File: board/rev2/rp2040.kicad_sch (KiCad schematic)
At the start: 2 parts, among them U13 TLV74311, U5 RP2354B

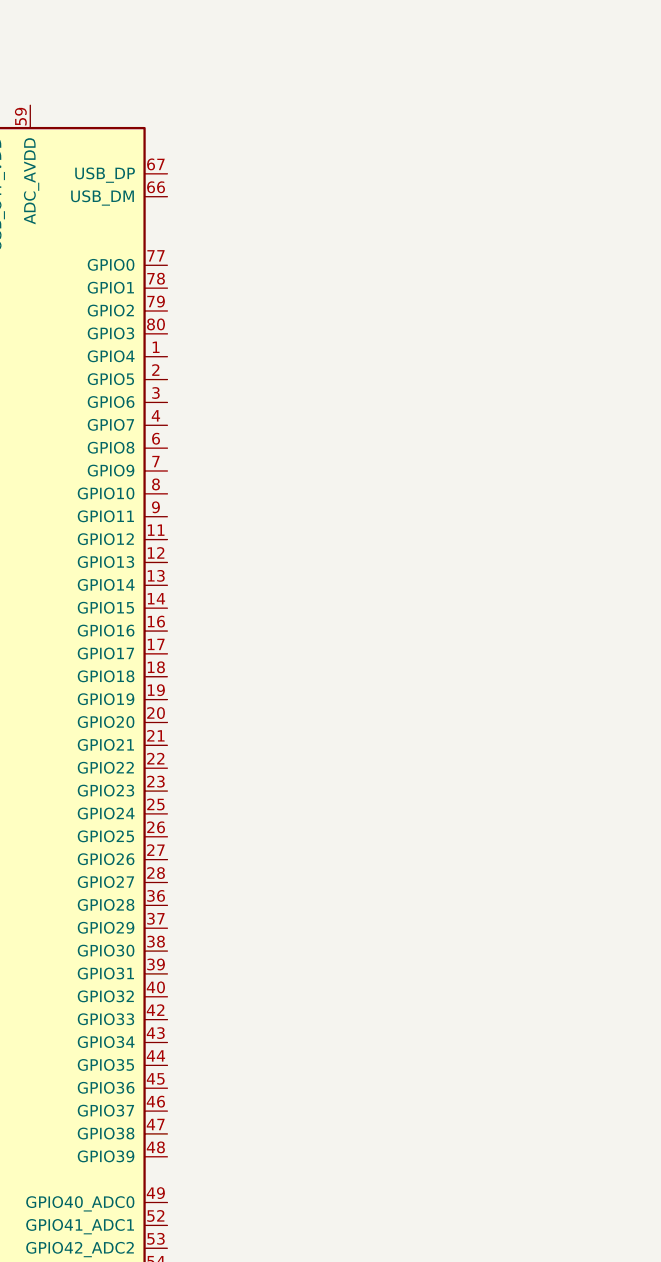
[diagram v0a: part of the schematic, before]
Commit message: Split out board into A/B
allow 2x displays (for chaining)
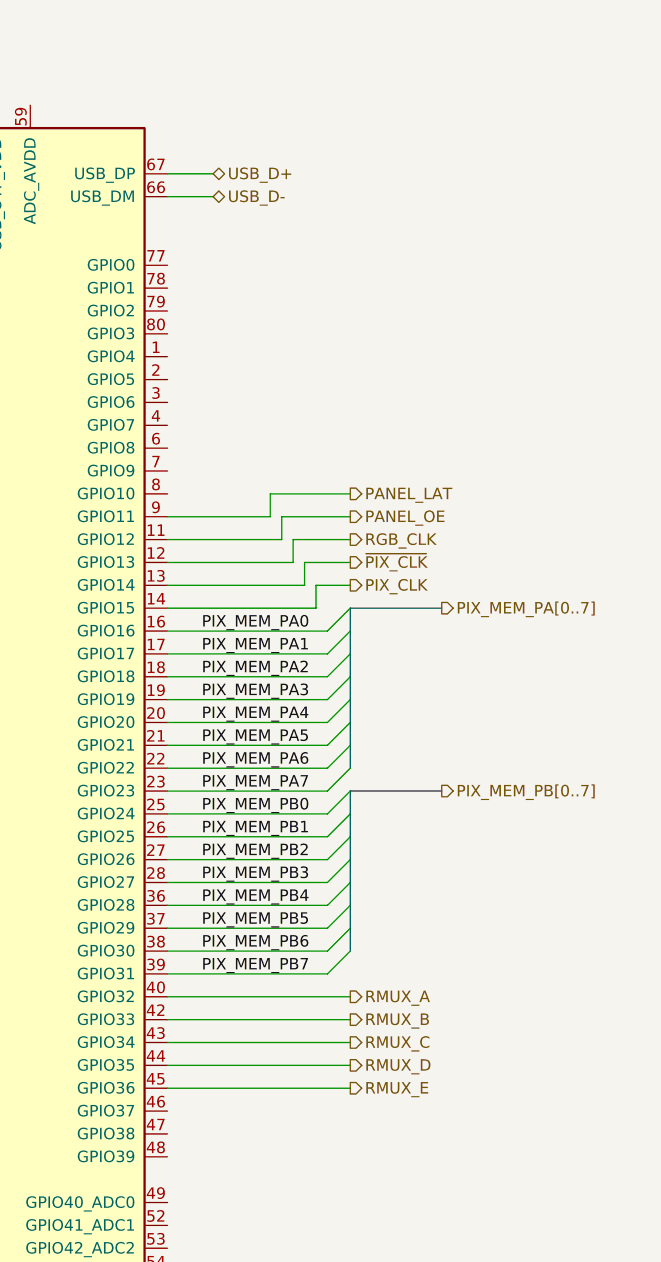
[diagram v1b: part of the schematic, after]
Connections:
- net PANEL_OE: now reaches U5.11 (GPIO12)
- net RGB_CLK: now reaches U5.12 (GPIO13)
- net ~{PIX_CLK}: now reaches U5.13 (GPIO14)
- net PIX_CLK: now reaches U5.14 (GPIO15)
- net PIX_MEM_PA0: now reaches U5.16 (GPIO16)
- net PIX_MEM_PA1: now reaches U5.17 (GPIO17)
- net PIX_MEM_PA2: now reaches U5.18 (GPIO18)
- net PIX_MEM_PA3: now reaches U5.19 (GPIO19)
- net PIX_MEM_PA4: now reaches U5.20 (GPIO20)
- net PIX_MEM_PA5: now reaches U5.21 (GPIO21)
- net PIX_MEM_PA6: now reaches U5.22 (GPIO22)
- net PIX_MEM_PA7: now reaches U5.23 (GPIO23)
- net PIX_MEM_PB0: now reaches U5.25 (GPIO24)
- net PIX_MEM_PB1: now reaches U5.26 (GPIO25)
- net PIX_MEM_PB2: now reaches U5.27 (GPIO26)
- net PIX_MEM_PB3: now reaches U5.28 (GPIO27)
- net PIX_MEM_PB4: now reaches U5.36 (GPIO28)
- net PIX_MEM_PB5: now reaches U5.37 (GPIO29)
- net PIX_MEM_PB6: now reaches U5.38 (GPIO30)
- net PIX_MEM_PB7: now reaches U5.39 (GPIO31)
- net RMUX_A: now reaches U5.40 (GPIO32)
- net RMUX_B: now reaches U5.42 (GPIO33)
- net RMUX_C: now reaches U5.43 (GPIO34)
- net RMUX_D: now reaches U5.44 (GPIO35)
- net RMUX_E: now reaches U5.45 (GPIO36)
- net USB_D-: now reaches U5.66 (USB_DM)
- net USB_D+: now reaches U5.67 (USB_DP)
- net PANEL_LAT: now reaches U5.9 (GPIO11)

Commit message: More board work
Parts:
- added R30, R31: 10k, symbol Device:R_Small_US
- added R32: 1k, symbol Device:R_Small_US
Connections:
- net DAT0: now reaches U5.1 (GPIO4)
- net DAT3: now reaches U5.2 (GPIO5)
- net CLK: now reaches U5.3 (GPIO6)
- net CLK: now also U5.53 (GPIO42_ADC2)
- net CMD: now reaches U5.4 (GPIO7)
- net at U5.46 (GPIO37): now also R32.1
- net MEMA_WE: now reaches U5.47 (GPIO38)
- net MEMA_WE: now also R30.2
- net MEMB_WE: now reaches U5.48 (GPIO39)
- net MEMB_WE: now also R31.2
- net CS: now reaches U5.52 (GPIO41_ADC1)
- net Q0: now reaches U5.54 (GPIO43_ADC3)
- net Q1: now reaches U5.55 (GPIO44_ADC4)
- net Q2: now reaches U5.56 (GPIO45_ADC5)
- net Q3: now reaches U5.57 (GPIO46_ADC6)
- net PIX_CNT_DIN0: now reaches U5.77 (GPIO0)
- net PIX_CNT_DIN1: now reaches U5.78 (GPIO1)
- net PIX_CNT_DIN2: now reaches U5.79 (GPIO2)
- net PIX_CNT_DIN3: now reaches U5.80 (GPIO3)
- new net MEM_IO: R32.2
- new net VDD: R30.1, R31.1

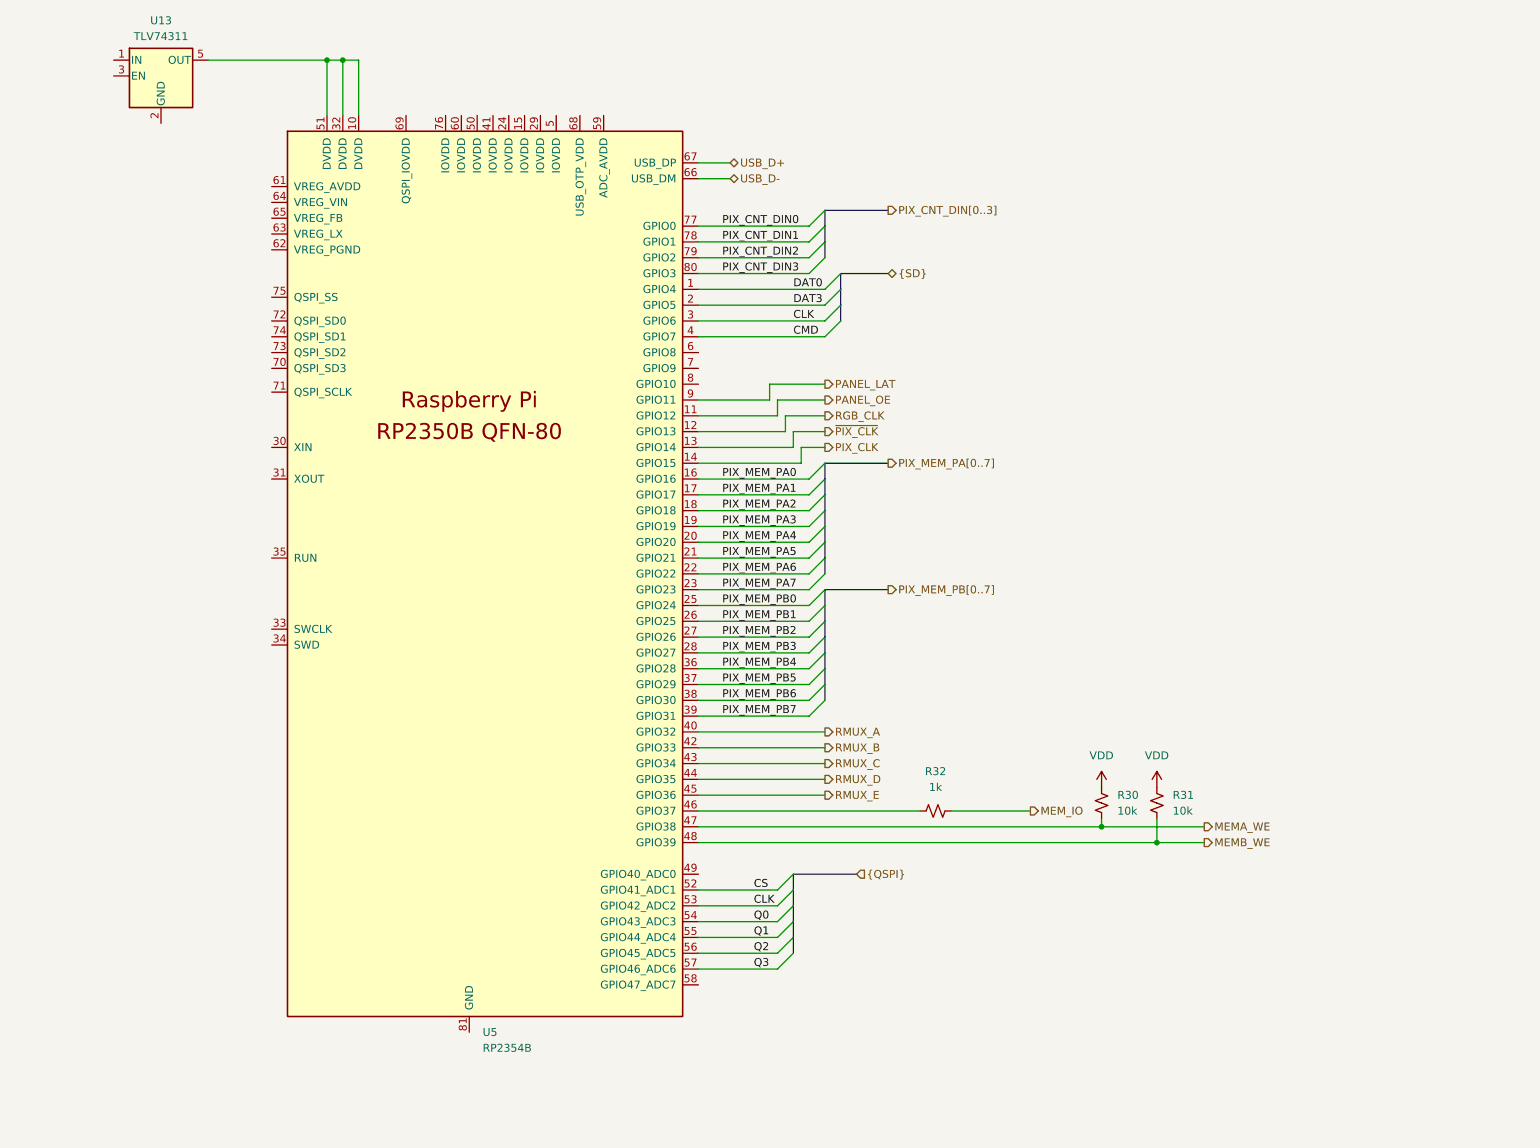
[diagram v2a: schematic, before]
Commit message: Board GPIO allocation
- and usbmux

still need to do termination on the big buses + a bunch of bypass caps
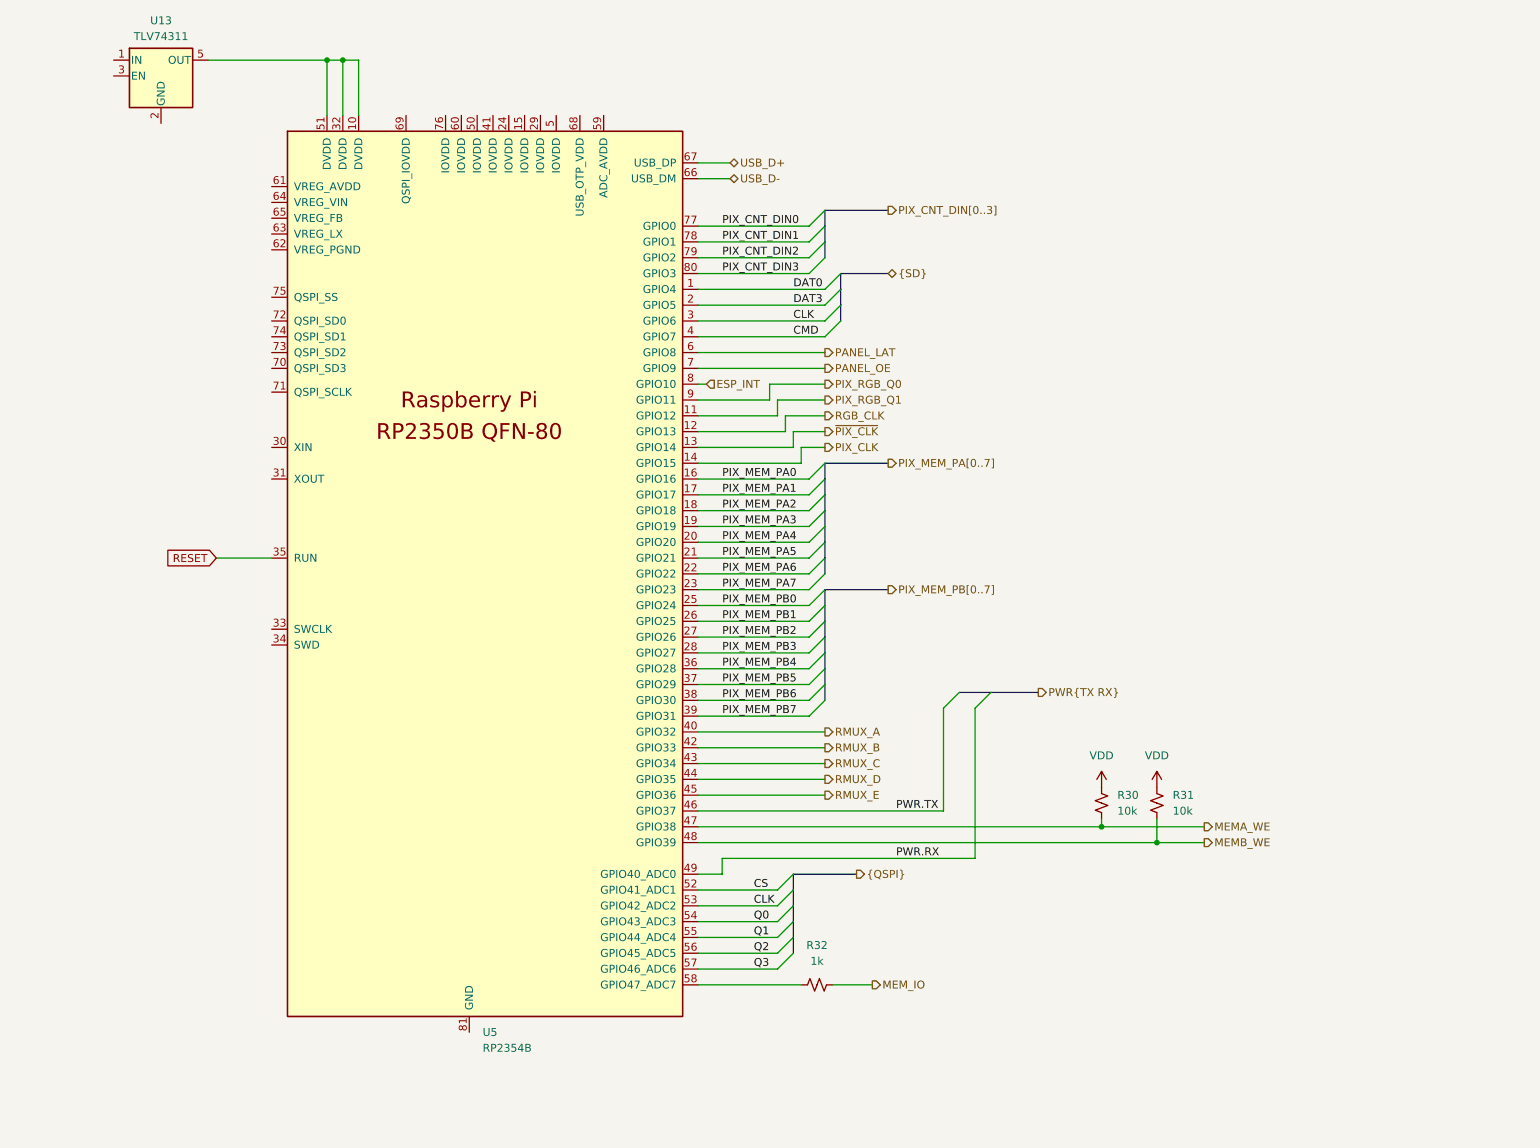
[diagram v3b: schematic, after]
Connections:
- net PANEL_LAT: now also U5.6 (GPIO8); no longer U5.9 (GPIO11)
- net PANEL_OE: now also U5.7 (GPIO9); no longer U5.11 (GPIO12)
- net RESET: now reaches U5.35 (RUN)
- net at R32.1: now also U5.58 (GPIO47_ADC7); no longer U5.46 (GPIO37)
- net PWR.RX: now reaches U5.49 (GPIO40_ADC0)
- net ESP_INT: now reaches U5.8 (GPIO10)
- new net PIX_RGB_Q0: U5.9 (GPIO11)
- new net PIX_RGB_Q1: U5.11 (GPIO12)
- new net PWR.TX: U5.46 (GPIO37)
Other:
- company: (none) -> MLABS
- title: (none) -> Main (Display) Microcontroller
- moved on the sheet: R32

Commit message: Continue board, assign caps/res, adjust for JLC availability
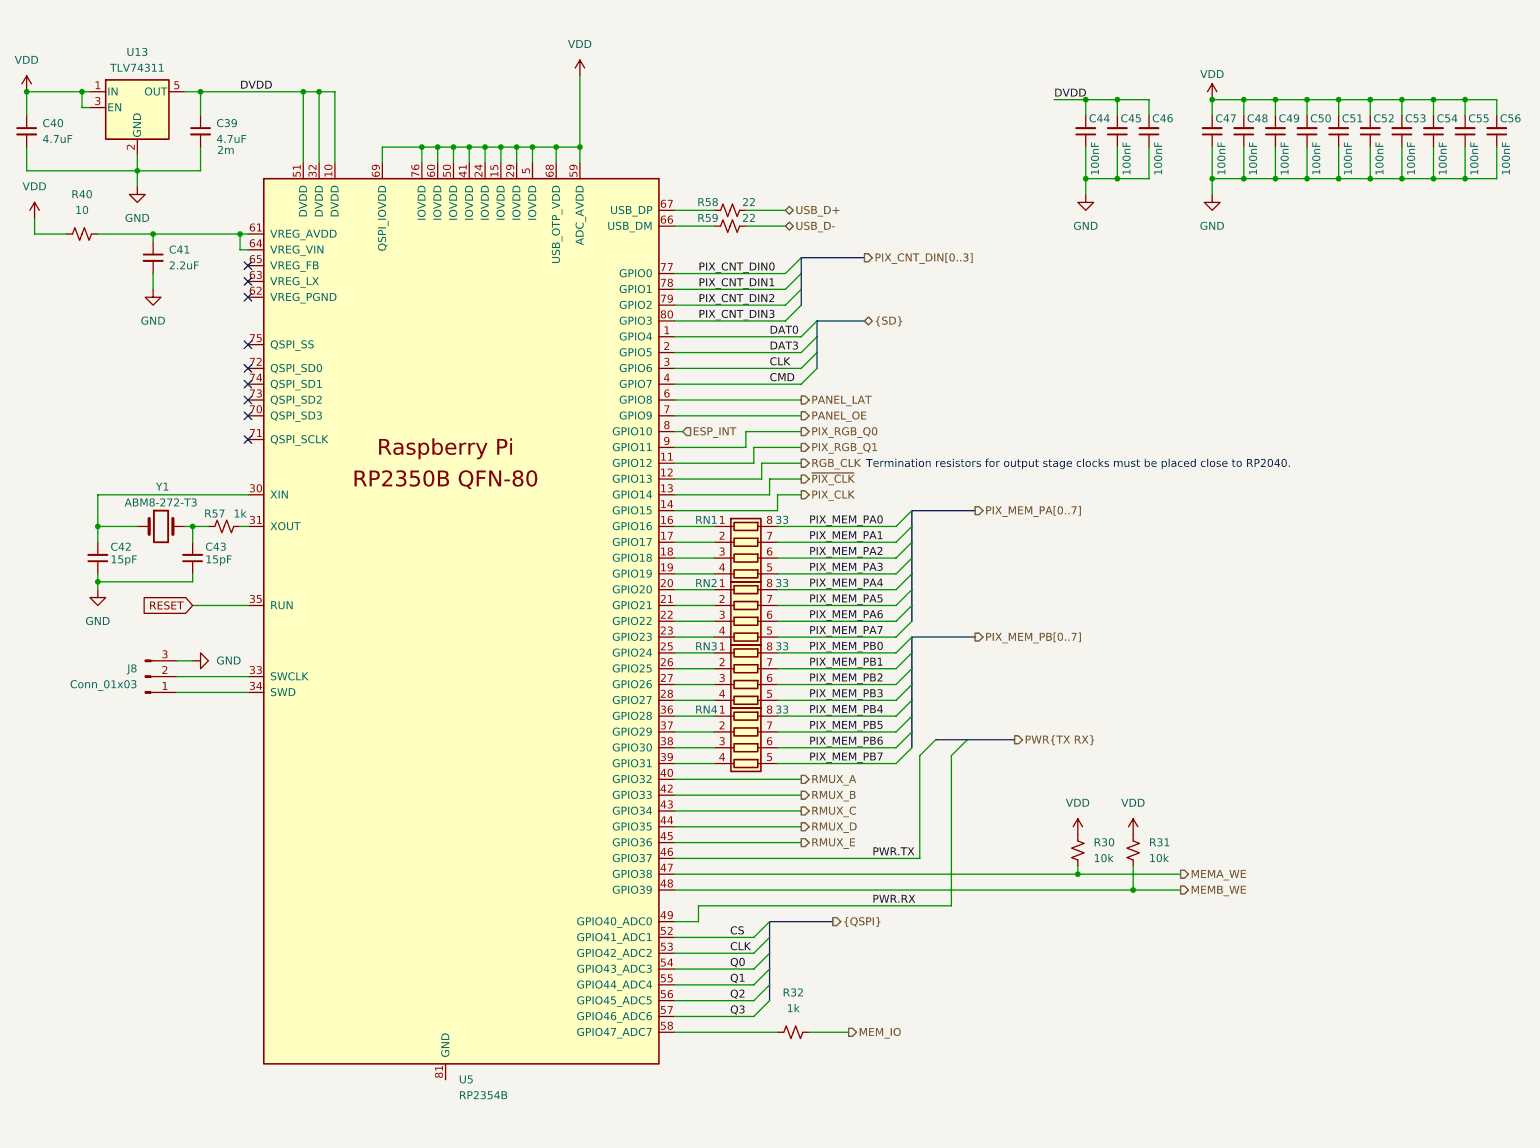
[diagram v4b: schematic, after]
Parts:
- added C39, C40: 4.7uF, Capacitor_SMD:C_1206_3216Metric, symbol Device:C_Small
- added C41: 2.2uF, Capacitor_SMD:C_0603_1608Metric, symbol Device:C_Small
- added C42, C43: 15pF, Capacitor_SMD:C_0402_1005Metric, symbol Device:C_Small
- added C44, C45, C46, C47, C48, C49, C50, C51, C52, C53, C54, C55, C56: 100nF, Capacitor_SMD:C_0402_1005Metric, symbol Device:C_Small
- added J8: Conn_01x03, Connector_PinHeader_2.54mm:PinHeader_1x03_P2.54mm_Vertical, symbol Connector:Conn_01x03_Pin
- added R40: 10, Resistor_SMD:R_0402_1005Metric, symbol Device:R_Small_US
- added R57: 1k, Resistor_SMD:R_0402_1005Metric, symbol Device:R_Small_US
- added R58, R59: 22, Resistor_SMD:R_0402_1005Metric, symbol Device:R_Small_US
- added RN1, RN2, RN3, RN4: 33, symbol Device:R_Pack04
- added Y1: ABM8-272-T3, Crystal:Crystal_SMD_3225-4Pin_3.2x2.5mm, symbol Device:Crystal
- R30, R31: footprint (none) -> Resistor_SMD:R_0805_2012Metric; Part (none) -> 0805W8F1002T5E
- R32: footprint (none) -> Resistor_SMD:R_0402_1005Metric; Part (none) -> 0402WGF1001TCE
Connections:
- net PIX_MEM_PA0: now also RN1.8 (R1.2); no longer U5.16 (GPIO16)
- net PIX_MEM_PA1: now also RN1.7 (R2.2); no longer U5.17 (GPIO17)
- net PIX_MEM_PA2: now also RN1.6 (R3.2); no longer U5.18 (GPIO18)
- net PIX_MEM_PA3: now also RN1.5 (R4.2); no longer U5.19 (GPIO19)
- net PIX_MEM_PA4: now also RN2.8 (R1.2); no longer U5.20 (GPIO20)
- net PIX_MEM_PA5: now also RN2.7 (R2.2); no longer U5.21 (GPIO21)
- net PIX_MEM_PA6: now also RN2.6 (R3.2); no longer U5.22 (GPIO22)
- net PIX_MEM_PA7: now also RN2.5 (R4.2); no longer U5.23 (GPIO23)
- net PIX_MEM_PB0: now also RN3.8 (R1.2); no longer U5.25 (GPIO24)
- net PIX_MEM_PB1: now also RN3.7 (R2.2); no longer U5.26 (GPIO25)
- net PIX_MEM_PB2: now also RN3.6 (R3.2); no longer U5.27 (GPIO26)
- net PIX_MEM_PB3: now also RN3.5 (R4.2); no longer U5.28 (GPIO27)
- net PIX_MEM_PB4: now also RN4.8 (R1.2); no longer U5.36 (GPIO28)
- net PIX_MEM_PB5: now also RN4.7 (R2.2); no longer U5.37 (GPIO29)
- net PIX_MEM_PB6: now also RN4.6 (R3.2); no longer U5.38 (GPIO30)
- net PIX_MEM_PB7: now also RN4.5 (R4.2); no longer U5.39 (GPIO31)
- net USB_D+: now also R58.2; no longer U5.67 (USB_DP)
- net USB_D-: now also R59.2; no longer U5.66 (USB_DM)
- net VDD: now also U13.1 (IN), U13.3 (EN), U5.15 (IOVDD), U5.24 (IOVDD), U5.29 (IOVDD), U5.41 (IOVDD), U5.5 (IOVDD), U5.50 (IOVDD), U5.59 (ADC_AVDD), U5.60 (IOVDD), U5.68 (USB_OTP_VDD), U5.69 (QSPI_IOVDD), U5.76 (IOVDD), C40.1, C47.2, C48.2, C49.2, C50.2, C51.2, C52.2, C53.2, C54.2, C55.2, C56.2, R40.1
- net GND: now reaches U13.2 (GND)
- net GND: now also C39.2, C40.2, C41.2, C42.1, C43.1, C44.1, C45.1, C46.1, C47.1, C48.1, C49.1, C50.1, C51.1, C52.1, C53.1, C54.1, C55.1, C56.1, J8.3 (Pin_3)
- net DVDD: now reaches U13.5 (OUT), U5.10 (DVDD), U5.32 (DVDD), U5.51 (DVDD)
- net DVDD: now also C39.1, C44.2, C45.2, C46.2
- net at U5.30 (XIN): now also C42.2, Y1.1
- net at U5.31 (XOUT): now also R57.2
- net at U5.33 (SWCLK): now also J8.2 (Pin_2)
- net at U5.34 (SWD): now also J8.1 (Pin_1)
- net at U5.61 (VREG_AVDD): now also U5.64 (VREG_VIN), C41.1, R40.2
- new net: RN2.1 (R1.1), U5.20 (GPIO20)
- new net: RN2.2 (R2.1), U5.21 (GPIO21)
- new net: RN2.3 (R3.1), U5.22 (GPIO22)
- new net: RN2.4 (R4.1), U5.23 (GPIO23)
- new net: C43.2, R57.1, Y1.2
- new net: R58.1, U5.67 (USB_DP)
- new net: RN1.1 (R1.1), U5.16 (GPIO16)
- new net: RN1.2 (R2.1), U5.17 (GPIO17)
- new net: RN1.3 (R3.1), U5.18 (GPIO18)
- new net: RN1.4 (R4.1), U5.19 (GPIO19)
- new net: RN3.1 (R1.1), U5.25 (GPIO24)
- new net: RN3.2 (R2.1), U5.26 (GPIO25)
- new net: RN3.3 (R3.1), U5.27 (GPIO26)
- new net: RN3.4 (R4.1), U5.28 (GPIO27)
- new net: RN4.1 (R1.1), U5.36 (GPIO28)
- new net: RN4.2 (R2.1), U5.37 (GPIO29)
- new net: RN4.3 (R3.1), U5.38 (GPIO30)
- new net: RN4.4 (R4.1), U5.39 (GPIO31)
- new net: R59.1, U5.66 (USB_DM)
- no-connect marks 0 -> 9
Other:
- note added: "Termination resistors for output stage clocks must be placed close to RP2040."
- moved on the sheet: R30, R31, R32, U13, U5
